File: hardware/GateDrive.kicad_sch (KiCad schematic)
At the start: 15 parts, among them U6 DRV8323RSRGZT

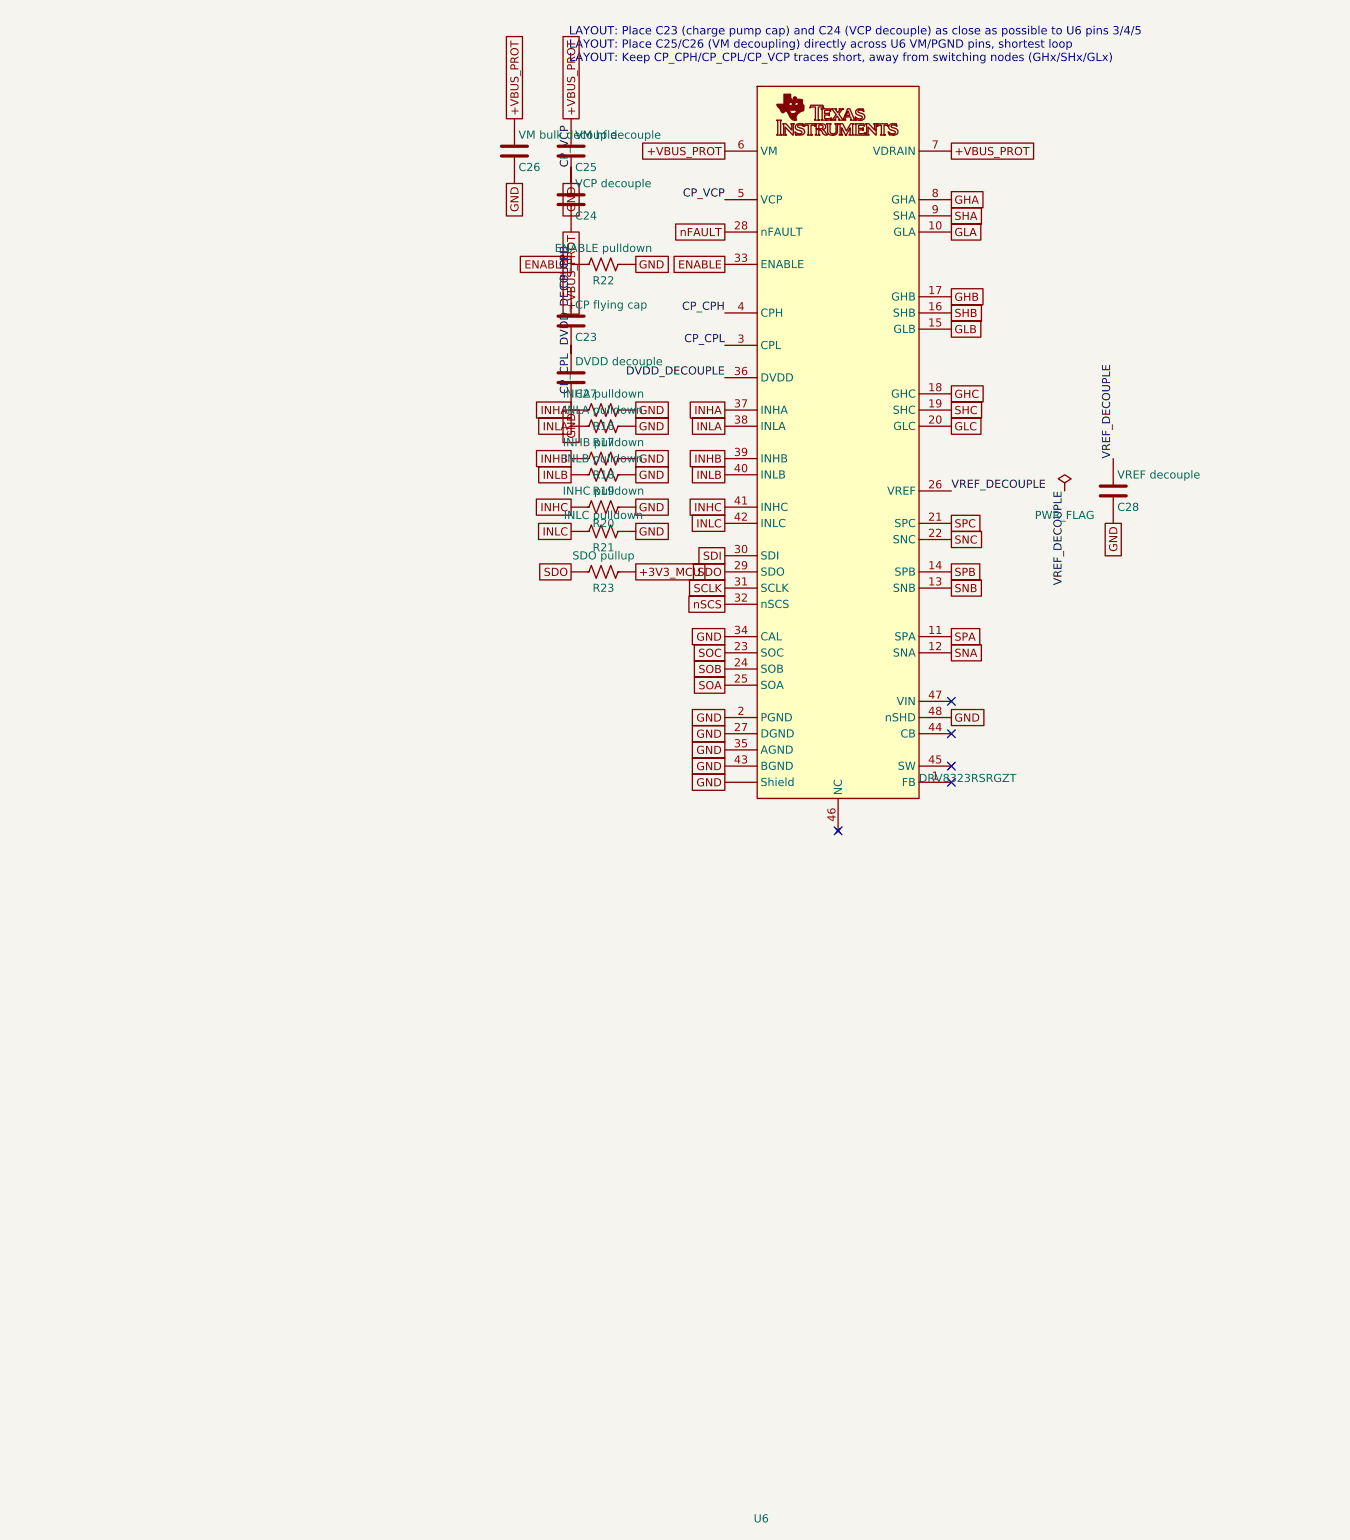
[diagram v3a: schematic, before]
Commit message: Schematic Rev B: full rebuild per METU PowerLab rules
Rev A was withdrawn: labels stuck on pins created real net shorts
(+5V_LOGIC with the 36 V bus, INHA and EFUSE_IMON with GND) and several
circuits contradicted their datasheets.

Rev B: real wires and power symbols on the 2.54 mm grid, hierarchical sheets
(half bridge reused 3x), library values, LAYOUT notes, root page with specs
and block diagram. Circuit fixes: DRV8323 VREF driven, unused buck tied to
GND, INA240A1, LM74700-Q1 reverse polarity, SMBJ36CA, eFuse per datasheet,
direct 3.3 V buck, 4.7 uH/8.1 A inductor, 2512 shunts with net-tie Kelvin,
24 V CAN ESD. kicad-cli ERC: 0 errors; netlist matches intent on all nets.
Old board and project-local library tables removed (board is rebuilt next).

Co-Authored-By: Claude Opus 5.5 <noreply@anthropic.com>
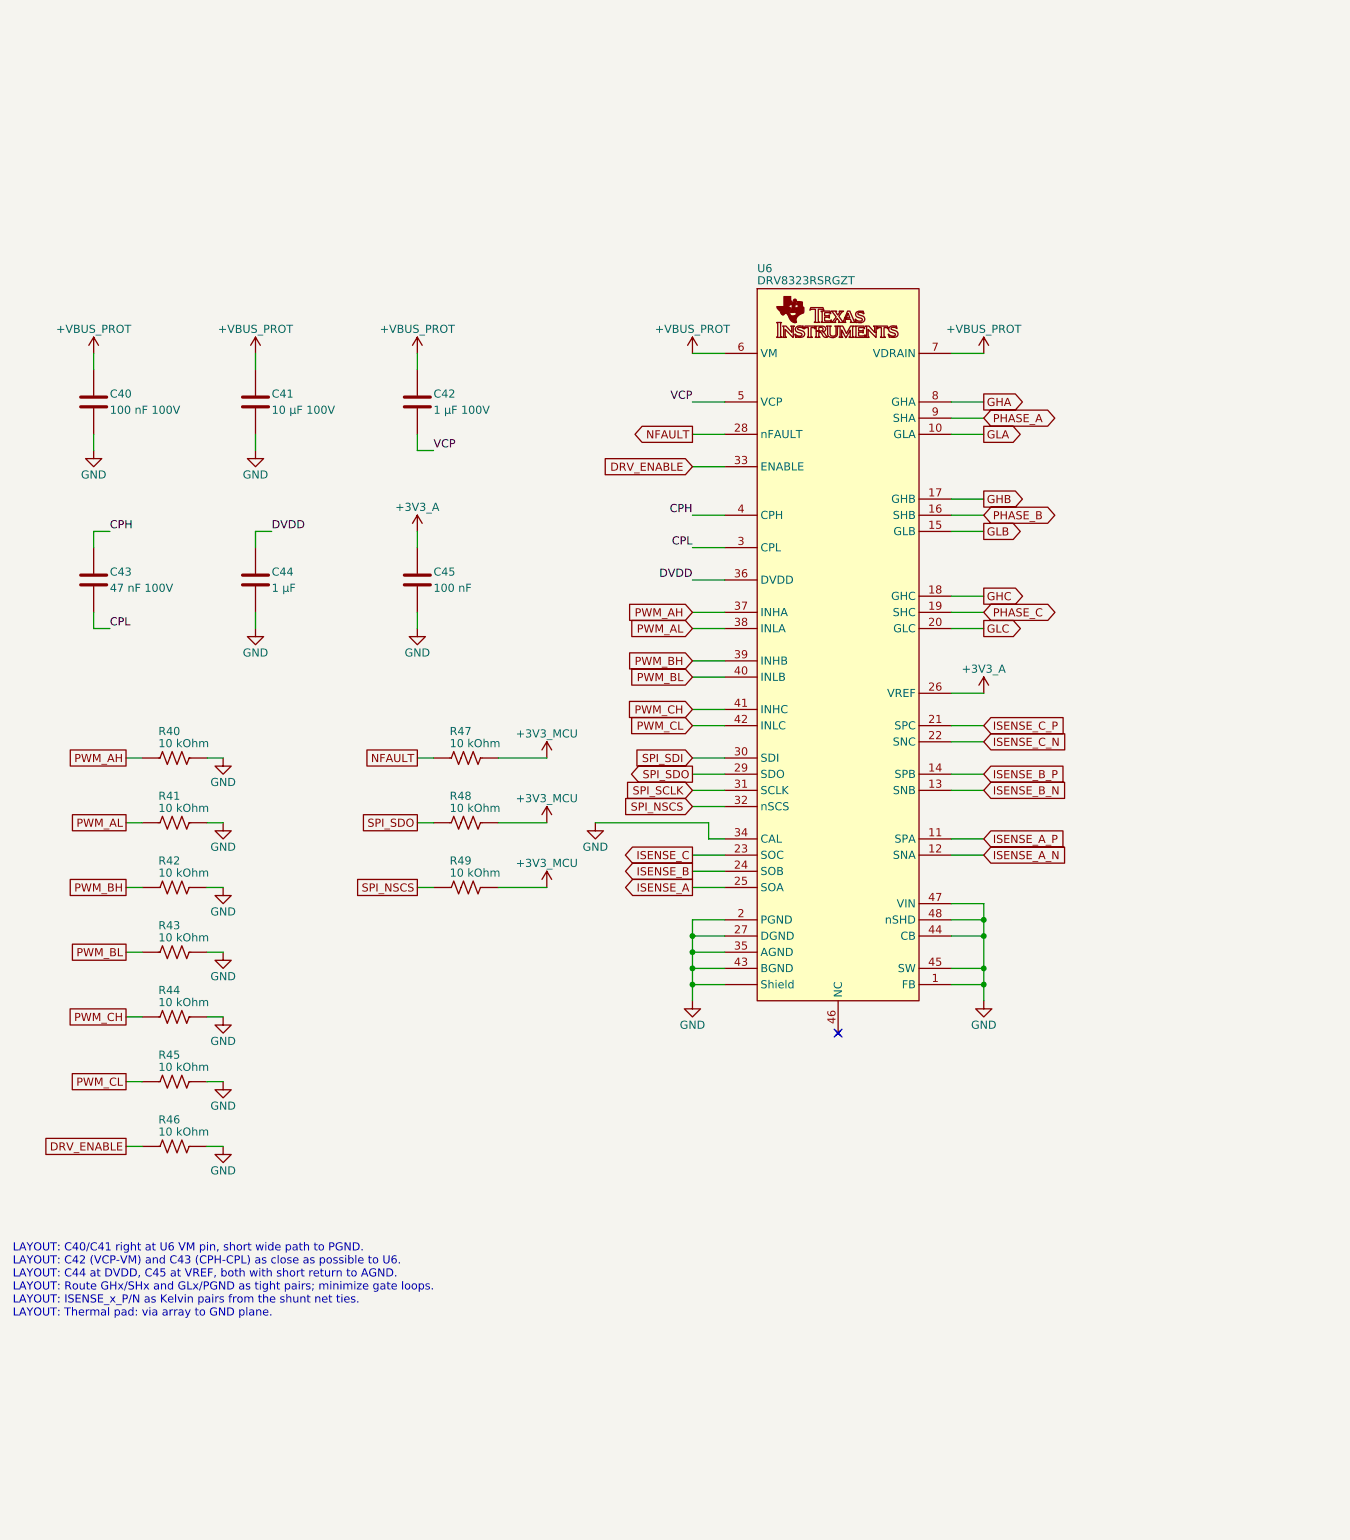
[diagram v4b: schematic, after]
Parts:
- removed C23: CP flying cap, METUPowerLab_Capacitors_Ceramics_SurfaceMounts:0805_Medium, symbol METUPowerLab_Capacitors_Ceramics_SurfaceMounts:47 nF 100V
- removed C24: VCP decouple, METUPowerLab_Capacitors_Ceramics_SurfaceMounts:0603_Medium, symbol METUPowerLab_Capacitors_Ceramics_SurfaceMounts:1 µF
- removed C25: VM hf decouple, METUPowerLab_Capacitors_Ceramics_SurfaceMounts:0603_Medium, symbol METUPowerLab_Capacitors_Ceramics_SurfaceMounts:100 nF
- removed C26: VM bulk decouple, METUPowerLab_Capacitors_Ceramics_SurfaceMounts:2220, symbol METUPowerLab_Capacitors_Ceramics_SurfaceMounts:10 µF 75V
- removed C27: DVDD decouple, METUPowerLab_Capacitors_Ceramics_SurfaceMounts:0603_Medium, symbol METUPowerLab_Capacitors_Ceramics_SurfaceMounts:1 µF
- removed C28: VREF decouple, METUPowerLab_Capacitors_Ceramics_SurfaceMounts:0603_Medium, symbol METUPowerLab_Capacitors_Ceramics_SurfaceMounts:100 nF
- removed R16: INHA pulldown, METUPowerLab_Resistors_ChipResistors:0603_Medium, symbol METUPowerLab_Resistors_ChipResistors:10 kOhm
- removed R17: INLA pulldown, METUPowerLab_Resistors_ChipResistors:0603_Medium, symbol METUPowerLab_Resistors_ChipResistors:10 kOhm
- removed R18: INHB pulldown, METUPowerLab_Resistors_ChipResistors:0603_Medium, symbol METUPowerLab_Resistors_ChipResistors:10 kOhm
- removed R19: INLB pulldown, METUPowerLab_Resistors_ChipResistors:0603_Medium, symbol METUPowerLab_Resistors_ChipResistors:10 kOhm
- removed R20: INHC pulldown, METUPowerLab_Resistors_ChipResistors:0603_Medium, symbol METUPowerLab_Resistors_ChipResistors:10 kOhm
- removed R21: INLC pulldown, METUPowerLab_Resistors_ChipResistors:0603_Medium, symbol METUPowerLab_Resistors_ChipResistors:10 kOhm
- removed R22: ENABLE pulldown, METUPowerLab_Resistors_ChipResistors:0603_Medium, symbol METUPowerLab_Resistors_ChipResistors:10 kOhm
- removed R23: SDO pullup, METUPowerLab_Resistors_ChipResistors:0603_Medium, symbol METUPowerLab_Resistors_ChipResistors:10 kOhm
- added C40: 100 nF 100V, METUPowerLab_Capacitors_Ceramics_SurfaceMounts:0603_Medium, symbol METUPowerLab_Capacitors_Ceramics_SurfaceMounts:100 nF 100V
- added C41: 10 µF 100V, METUPowerLab_Capacitors_Ceramics_SurfaceMounts:1206_Medium, symbol METUPowerLab_Capacitors_Ceramics_SurfaceMounts:10 µF 100V 1206
- added C42: 1 µF 100V, METUPowerLab_Capacitors_Ceramics_SurfaceMounts:0603_Medium, symbol METUPowerLab_Capacitors_Ceramics_SurfaceMounts:1 µF 0603
- added C43: 47 nF 100V, METUPowerLab_Capacitors_Ceramics_SurfaceMounts:0603_Medium, symbol METUPowerLab_Capacitors_Ceramics_SurfaceMounts:47 nF 100V
- added C44: 1 µF, METUPowerLab_Capacitors_Ceramics_SurfaceMounts:0603_Medium, symbol METUPowerLab_Capacitors_Ceramics_SurfaceMounts:1 µF 0603
- added C45: 100 nF, METUPowerLab_Capacitors_Ceramics_SurfaceMounts:0603_Medium, symbol METUPowerLab_Capacitors_Ceramics_SurfaceMounts:100 nF
- added R40, R41, R42, R43, R44, R45, R46, R47, R48, R49: 10 kOhm, METUPowerLab_Resistors_ChipResistors:0603_Medium, symbol METUPowerLab_Resistors_ChipResistors:10 kOhm
- U6: Digi-Key Number (none) -> 296-46943-1-ND; Farnell Number (none) -> 3118809; Function (none) -> Controller - Commutation, Direction Management; Interface (none) -> SPI; Manufacturer (none) -> Texas Instruments; Manufacturer Number (none) -> DRV8323RSRGZT; Motor Type (none) -> BLDC; Mounting Type (none) -> Surface Mount; Mouser Number (none) -> 595-DRV8323RSRGZT; Operating Temperature (none) -> -40°C up to 125°C (TA); Output Configuration (none) -> Half Bridge; Package (none) -> 48-VQFN; Supply Voltage Rating (none) -> 6V up to 60V; Özdisan Number (none) -> DRV8323RSRGZT
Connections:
- net +3V3_MCU: now also R47.2, R48.2, R49.2
- net +VBUS_PROT: now also C40.1, C41.1, C42.1
- net GND: now also U6.1 (FB), U6.44 (CB), U6.45 (SW), U6.47 (VIN), C40.2, C41.2, C44.2, C45.2, R40.2, R41.2, R42.2, R43.2, R44.2, R45.2, R46.2; no longer U6.37 (INHA)
- net CP_CPH renamed CPH
- net CPH: now also C43.1
- net CP_CPL renamed CPL
- net CPL: now also C43.2
- net CP_VCP renamed VCP
- net VCP: now also C42.2
- net DVDD_DECOUPLE renamed DVDD
- net DVDD: now also C44.1
- net ENABLE renamed DRV_ENABLE
- net DRV_ENABLE: now also R46.1
- net INHB renamed PWM_BH
- net PWM_BH: now also R42.1
- net INHC renamed PWM_CH
- net PWM_CH: now also R44.1
- net INLA renamed PWM_AL
- net PWM_AL: now also R41.1
- net INLB renamed PWM_BL
- net PWM_BL: now also R43.1
- net INLC renamed PWM_CL
- net PWM_CL: now also R45.1
- net SCLK renamed SPI_SCLK
- net SDI renamed SPI_SDI
- net SDO renamed SPI_SDO
- net SPI_SDO: now also R48.1
- net SHA renamed PHASE_A
- net SHB renamed PHASE_B
- net SHC renamed PHASE_C
- net SNA renamed ISENSE_A_N
- net SNB renamed ISENSE_B_N
- net SNC renamed ISENSE_C_N
- net SOA renamed ISENSE_A
- net SOB renamed ISENSE_B
- net SOC renamed ISENSE_C
- net SPA renamed ISENSE_A_P
- net SPB renamed ISENSE_B_P
- net SPC renamed ISENSE_C_P
- net VREF_DECOUPLE renamed +3V3_A
- net +3V3_A: now also C45.1
- net nFAULT renamed NFAULT
- net NFAULT: now also R47.1
- net nSCS renamed SPI_NSCS
- net SPI_NSCS: now also R49.1
- new net PWM_AH: R40.1, U6.37 (INHA)
- no-connect marks 5 -> 1
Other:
- note added: "LAYOUT: C40/C41 right at U6 VM pin, short wide path to PGND. LAYOUT: C42 (VCP-VM) and C43 (CPH-CPL) as close as possible to U6. LAYOUT: C44 at DVDD, C45 at VREF, both with short return to AGND. LAYOUT: Route GHx/SHx and GLx/PGND as tight pairs; minimize gate loops. LAYOUT: ISENSE_x_P/N as Kelvin pairs from the shunt net ties. LAYOUT: Thermal pad: via array to GND plane."
- note removed: "LAYOUT: Place C23 (charge pump cap) and C24 (VCP decouple) as close as possible to U6 pins 3/4/5 LAYOUT: Place C25/C26 (VM decoupling) directly across U6 VM/PGND pins, shortest loop LAYOUT: Keep CP_CPH/CP_CPL/CP_VCP traces short, away from switching nodes (GHx/SHx/GLx)"
- title: ${PROJECT_NAME} -> Gate Drive
